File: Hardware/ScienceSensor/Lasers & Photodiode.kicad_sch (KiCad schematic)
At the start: 12 parts

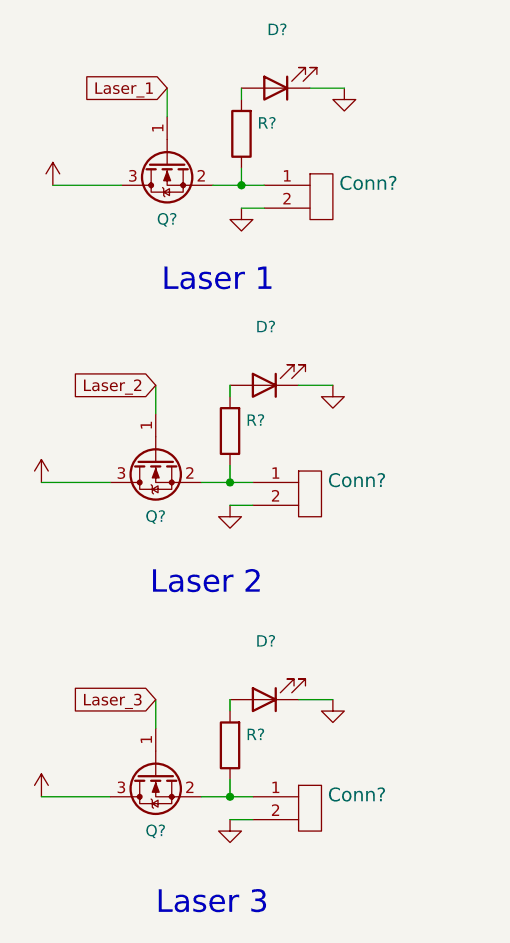
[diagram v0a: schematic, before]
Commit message: Created NO sensor, NH3 sensor, worked on Mosfets, and created Methane sensor with labels.
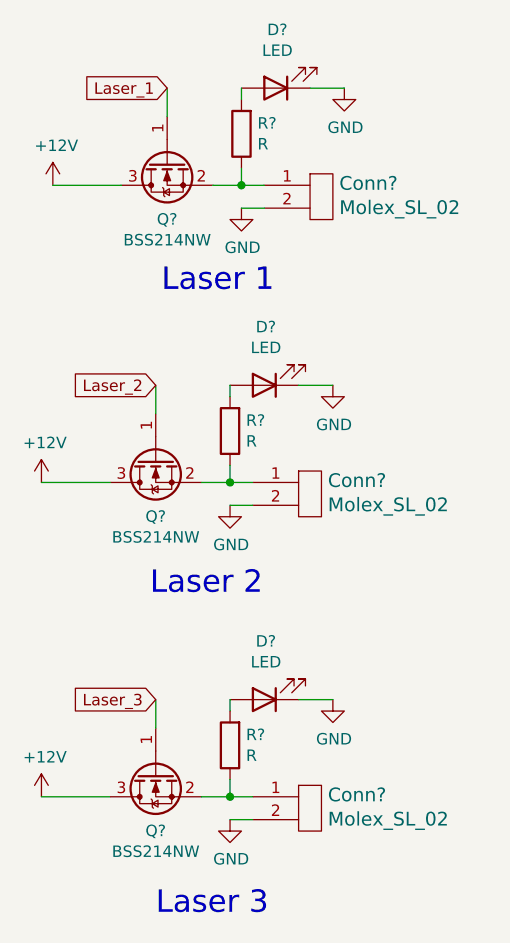
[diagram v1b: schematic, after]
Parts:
- Conn? (x3): value (none) -> Molex_SL_02
- D? (x3): value (none) -> LED
- Q? (x3): value (none) -> BSS214NW; footprint (none) -> Package_TO_SOT_SMD:SOT-323_SC-70
- R? (x3): value (none) -> R
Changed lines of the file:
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@@
     (in_bom yes) (on_board yes)
     (property "Reference" "Q?" (id 0) (at 38.1 42.5196 90))
-    (property "Value" "" (id 1) (at 38.1 44.831 90))
-    (property "Footprint" "" (id 2) (at 40.005 41.275 0)
+    (property "Value" "BSS214NW" (id 1) (at 38.1 44.831 90))
+    (property "Footprint" "Package_TO_SOT_SMD:SOT-323_SC-70" (id 2) (at 40.005 41.275 0)
       (effects (font (size 1.27 1.27) italic) (justify left) hide)
     )
@@
       (effects (font (size 1.524 1.524)) (justify left))
     )
-    (property "Value" "" (id 1) (at 57.2262 41.2242 0)
+    (property "Value" "Molex_SL_02" (id 1) (at 57.2262 41.2242 0)
       (effects (font (size 1.524 1.524)) (justify left))
     )
@@
       (effects (font (size 1.27 1.27)) hide)
     )
-    (property "Value" "" (id 1) (at 25.781 34.3408 0))
+    (property "Value" "+12V" (id 1) (at 25.781 34.3408 0))
     (property "Footprint" "" (id 2) (at 25.4 38.735 0)
       (effects (font (size 1.27 1.27)) hide)
@@
       (effects (font (size 1.27 1.27)) hide)
     )
-    (property "Value" "" (id 1) (at 46.482 45.6692 0))
+    (property "Value" "GND" (id 1) (at 46.482 45.6692 0))
     (property "Footprint" "" (id 2) (at 46.355 41.275 0)
       (effects (font (size 1.27 1.27)) hide)
@@
       (effects (font (size 1.27 1.27)) (justify right))
     )
-    (property "Value" "" (id 1) (at 48.133 34.163 0)
+    (property "Value" "R" (id 1) (at 48.133 34.163 0)
       (effects (font (size 1.27 1.27)) (justify right))
     )
@@
     (in_bom yes) (on_board yes)
     (property "Reference" "D?" (id 0) (at 50.3428 21.463 0))
-    (property "Value" "" (id 1) (at 50.3428 23.7744 0))
+    (property "Value" "LED" (id 1) (at 50.3428 23.7744 0))
     (property "Footprint" "" (id 2) (at 50.165 27.94 0)
       (effects (font (size 1.27 1.27)) hide)
@@
       (effects (font (size 1.27 1.27)) hide)
     )
-    (property "Value" "" (id 1) (at 57.912 32.3342 0))
+    (property "Value" "GND" (id 1) (at 57.912 32.3342 0))
     (property "Footprint" "" (id 2) (at 57.785 27.94 0)
       (effects (font (size 1.27 1.27)) hide)
@@
     (in_bom yes) (on_board yes)
     (property "Reference" "Q?" (id 0) (at 36.83 75.5396 90))
-    (property "Value" "" (id 1) (at 36.83 77.851 90))
-    (property "Footprint" "" (id 2) (at 38.735 74.295 0)
+    (property "Value" "BSS214NW" (id 1) (at 36.83 77.851 90))
+    (property "Footprint" "Package_TO_SOT_SMD:SOT-323_SC-70" (id 2) (at 38.735 74.295 0)
       (effects (font (size 1.27 1.27) italic) (justify left) hide)
     )
@@
       (effects (font (size 1.524 1.524)) (justify left))
     )
-    (property "Value" "" (id 1) (at 55.9562 74.2442 0)
+    (property "Value" "Molex_SL_02" (id 1) (at 55.9562 74.2442 0)
       (effects (font (size 1.524 1.524)) (justify left))
     )
@@
       (effects (font (size 1.27 1.27)) hide)
     )
-    (property "Value" "" (id 1) (at 24.511 67.3608 0))
+    (property "Value" "+12V" (id 1) (at 24.511 67.3608 0))
     (property "Footprint" "" (id 2) (at 24.13 71.755 0)
       (effects (font (size 1.27 1.27)) hide)
@@
       (effects (font (size 1.27 1.27)) hide)
     )
-    (property "Value" "" (id 1) (at 45.212 78.6892 0))
+    (property "Value" "GND" (id 1) (at 45.212 78.6892 0))
     (property "Footprint" "" (id 2) (at 45.085 74.295 0)
       (effects (font (size 1.27 1.27)) hide)
@@
       (effects (font (size 1.27 1.27)) (justify right))
     )
-    (property "Value" "" (id 1) (at 46.863 67.183 0)
+    (property "Value" "R" (id 1) (at 46.863 67.183 0)
       (effects (font (size 1.27 1.27)) (justify right))
     )
@@
     (in_bom yes) (on_board yes)
     (property "Reference" "D?" (id 0) (at 49.0728 54.483 0))
-    (property "Value" "" (id 1) (at 49.0728 56.7944 0))
+    (property "Value" "LED" (id 1) (at 49.0728 56.7944 0))
     (property "Footprint" "" (id 2) (at 48.895 60.96 0)
       (effects (font (size 1.27 1.27)) hide)
@@
       (effects (font (size 1.27 1.27)) hide)
     )
-    (property "Value" "" (id 1) (at 56.642 65.3542 0))
+    (property "Value" "GND" (id 1) (at 56.642 65.3542 0))
     (property "Footprint" "" (id 2) (at 56.515 60.96 0)
       (effects (font (size 1.27 1.27)) hide)
@@
     (in_bom yes) (on_board yes)
     (property "Reference" "Q?" (id 0) (at 36.83 110.4646 90))
-    (property "Value" "" (id 1) (at 36.83 112.776 90))
-    (property "Footprint" "" (id 2) (at 38.735 109.22 0)
+    (property "Value" "BSS214NW" (id 1) (at 36.83 112.776 90))
+    (property "Footprint" "Package_TO_SOT_SMD:SOT-323_SC-70" (id 2) (at 38.735 109.22 0)
       (effects (font (size 1.27 1.27) italic) (justify left) hide)
     )
@@
       (effects (font (size 1.524 1.524)) (justify left))
     )
-    (property "Value" "" (id 1) (at 55.9562 109.1692 0)
+    (property "Value" "Molex_SL_02" (id 1) (at 55.9562 109.1692 0)
       (effects (font (size 1.524 1.524)) (justify left))
     )
@@
       (effects (font (size 1.27 1.27)) hide)
     )
-    (property "Value" "" (id 1) (at 24.511 102.2858 0))
+    (property "Value" "+12V" (id 1) (at 24.511 102.2858 0))
     (property "Footprint" "" (id 2) (at 24.13 106.68 0)
       (effects (font (size 1.27 1.27)) hide)
@@
       (effects (font (size 1.27 1.27)) hide)
     )
-    (property "Value" "" (id 1) (at 45.212 113.6142 0))
+    (property "Value" "GND" (id 1) (at 45.212 113.6142 0))
     (property "Footprint" "" (id 2) (at 45.085 109.22 0)
       (effects (font (size 1.27 1.27)) hide)
@@
       (effects (font (size 1.27 1.27)) (justify right))
     )
-    (property "Value" "" (id 1) (at 46.863 102.108 0)
+    (property "Value" "R" (id 1) (at 46.863 102.108 0)
       (effects (font (size 1.27 1.27)) (justify right))
     )
@@
     (in_bom yes) (on_board yes)
     (property "Reference" "D?" (id 0) (at 49.0728 89.408 0))
-    (property "Value" "" (id 1) (at 49.0728 91.7194 0))
+    (property "Value" "LED" (id 1) (at 49.0728 91.7194 0))
     (property "Footprint" "" (id 2) (at 48.895 95.885 0)
       (effects (font (size 1.27 1.27)) hide)
@@
       (effects (font (size 1.27 1.27)) hide)
     )
-    (property "Value" "" (id 1) (at 56.642 100.2792 0))
+    (property "Value" "GND" (id 1) (at 56.642 100.2792 0))
     (property "Footprint" "" (id 2) (at 56.515 95.885 0)
       (effects (font (size 1.27 1.27)) hide)

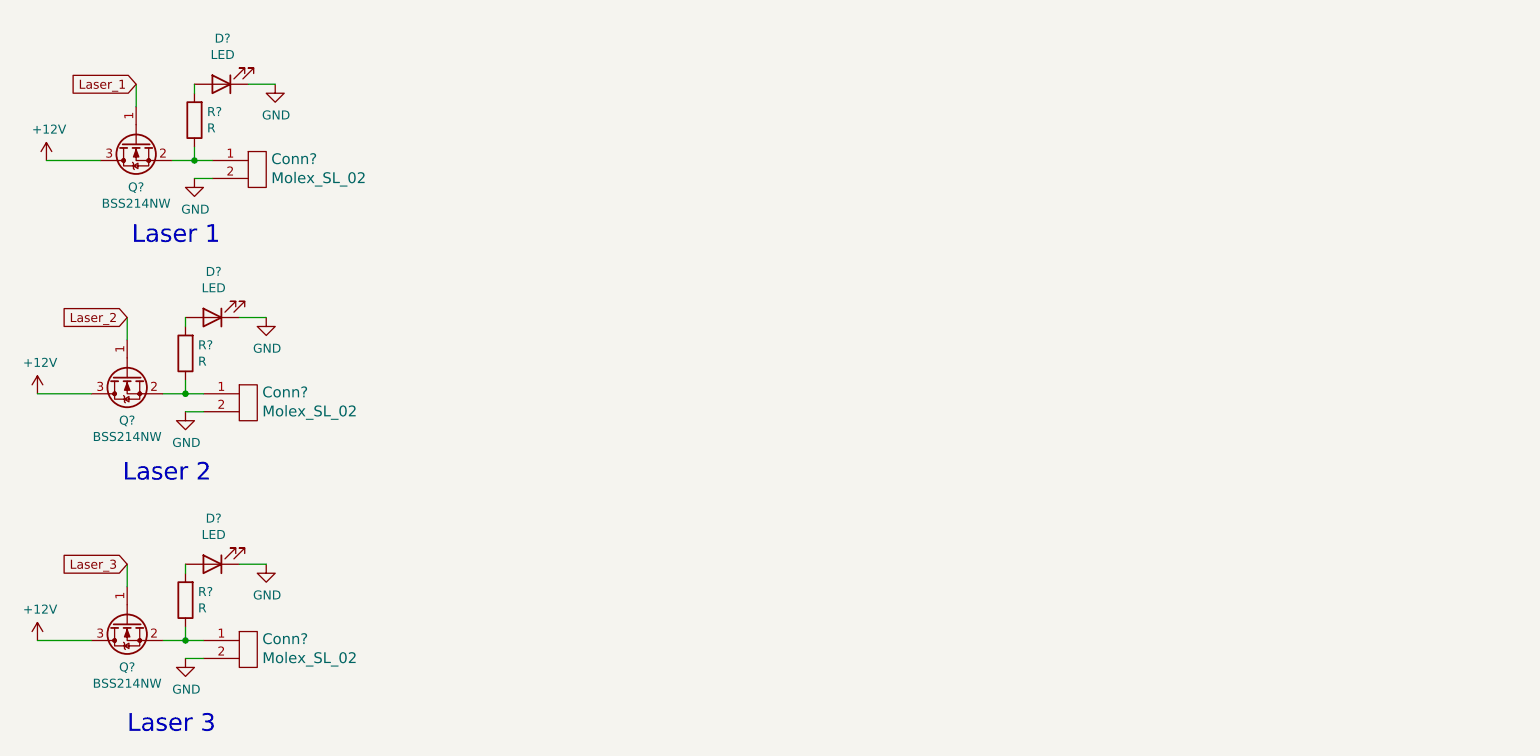
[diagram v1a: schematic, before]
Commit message: BOM generated, photodiodes added
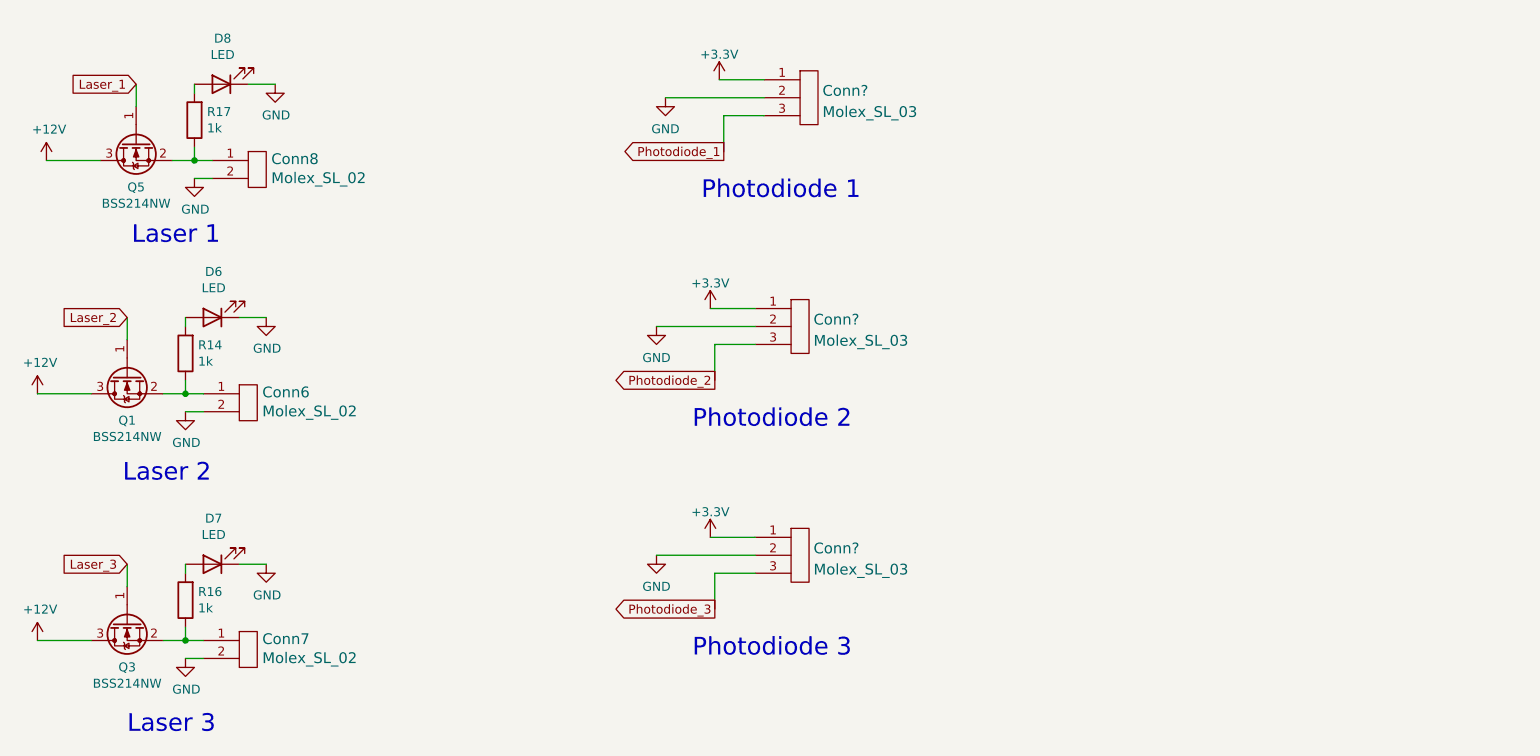
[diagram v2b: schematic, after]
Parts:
- added Conn? (x3): Molex_SL_03, symbol MRDT_Connectors:Molex_SL_03
- R14, R16, R17: renamed from R?; value R -> 1k
- gave numbers to parts that had none: 9
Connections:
- net GND: now also Conn?.2, Conn?.2, Conn?.2
- new net +3.3V: Conn?.1, Conn?.1, Conn?.1
- new net Photodiode_1: Conn?.3
- new net Photodiode_2: Conn?.3
- new net Photodiode_3: Conn?.3
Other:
- note added: "Photodiode 1"
- note added: "Photodiode 2"
- note added: "Photodiode 3"

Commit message: Fixed diode ref / values
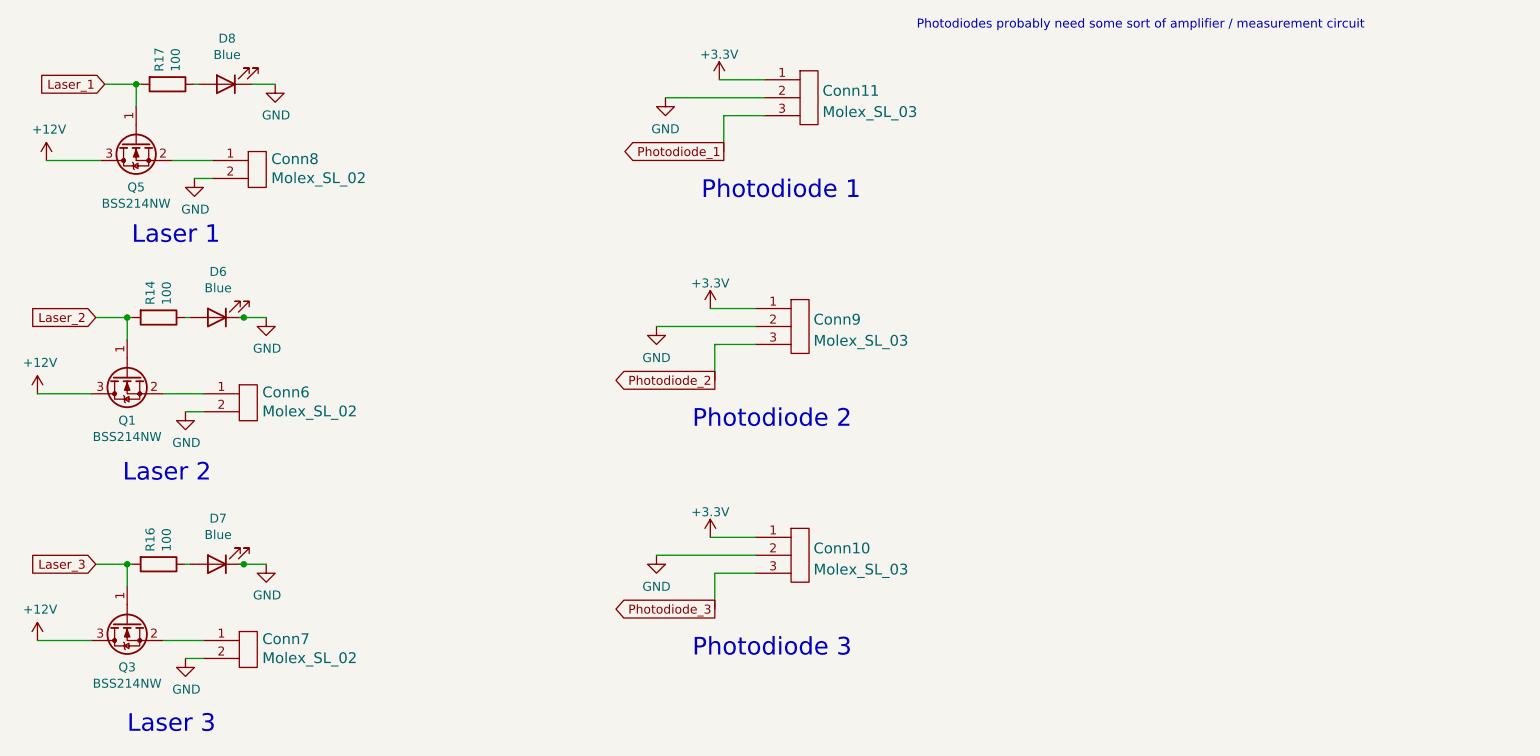
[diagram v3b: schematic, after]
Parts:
- D6, D7, D8: value LED -> Blue
- R14, R16, R17: value 1k -> 100
- gave numbers to parts that had none: 3
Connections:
- net Laser_1: now also R17.2
- net Laser_2: now also R14.2
- net Laser_3: now also R16.2
- net at Conn8.1, Q5.2 (S): no longer R17.1
- net at D8.2 (A): now also R17.1; no longer R17.2
- net at Conn6.1, Q1.2 (S): no longer R14.1
- net at D6.2 (A): now also R14.1; no longer R14.2
- net at Conn7.1, Q3.2 (S): no longer R16.1
- net at D7.2 (A): now also R16.1; no longer R16.2
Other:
- note added: "Photodiodes probably need some sort of amplifier / measurement circuit"
- moved on the sheet: D6, D7, D8, R14, R16, R17

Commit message: Schematic Review
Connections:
- net +12V: no longer Q5.3 (D)
- net GND: no longer Conn8.2
- net Laser_1: no longer Q5.1 (G)
- net at Q5.2 (S): no longer Conn8.1
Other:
- moved on the sheet: Q5
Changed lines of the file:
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@@
 (kicad_sch (version 20211123) (generator eeschema)
   (paper "A4")
-  (junction (at 38.1 27.94) (diameter 0) (color 0 0 0 0)
-  )
   (junction (at 36.83 60.96) (diameter 0) (color 0 0 0 0)
   )
@@
   (junction (at 53.34 60.96) (diameter 0) (color 0 0 0 0)
   )
-  (wire (pts (xy 33.655 27.94) (xy 38.1 27.94))
+  (wire (pts (xy 33.655 27.94) (xy 38.735 27.94))
     (stroke (width 0) (type default) (color 0 0 0 0))
   )
@@
     (stroke (width 0) (type default) (color 0 0 0 0))
   )
-  (wire (pts (xy 38.1 31.115) (xy 38.1 27.94))
-    (stroke (width 0) (type default) (color 0 0 0 0))
-  )
-  (wire (pts (xy 38.1 27.94) (xy 38.735 27.94))
-    (stroke (width 0) (type default) (color 0 0 0 0))
-  )
   (wire (pts (xy 120.65 27.305) (xy 127 27.305))
     (stroke (width 0) (type default) (color 0 0 0 0))
@@
     (stroke (width 0) (type default) (color 0 0 0 0))
   )
-  (wire (pts (xy 25.4 38.735) (xy 33.02 38.735))
-    (stroke (width 0) (type default) (color 0 0 0 0))
-  )
   (wire (pts (xy 45.085 74.295) (xy 47.625 74.295))
     (stroke (width 0) (type default) (color 0 0 0 0))
@@
   )
   (wire (pts (xy 121.285 32.385) (xy 121.285 37.465))
-    (stroke (width 0) (type default) (color 0 0 0 0))
-  )
-  (wire (pts (xy 43.18 38.735) (xy 48.895 38.735))
     (stroke (width 0) (type default) (color 0 0 0 0))
   )
@@
     )
   )
-  (symbol (lib_id "Transistor_FET:BSS214NW") (at 38.1 36.195 90) (mirror x) (unit 1)
-    (in_bom yes) (on_board yes)
-    (property "Reference" "Q5" (id 0) (at 38.1 42.5196 90))
-    (property "Value" "BSS214NW" (id 1) (at 38.1 44.831 90))
-    (property "Footprint" "Package_TO_SOT_SMD:SOT-323_SC-70" (id 2) (at 40.005 41.275 0)
+  (symbol (lib_id "Transistor_FET:BSS214NW") (at 35.56 36.195 0) (mirror x) (unit 1)
+    (in_bom yes) (on_board yes)
+    (property "Reference" "Q5" (id 0) (at 41.8846 36.195 90))
+    (property "Value" "BSS214NW" (id 1) (at 44.196 36.195 90))
+    (property "Footprint" "Package_TO_SOT_SMD:SOT-323_SC-70" (id 2) (at 40.64 34.29 0)
       (effects (font (size 1.27 1.27) italic) (justify left) hide)
     )
-    (property "Datasheet" "https://www.infineon.com/dgdl/Infineon-BSS214NW-DS-v02_02-en.pdf?fileId=db3a30431b3e89eb011b695aebc01bde" (id 3) (at 38.1 36.195 0)
+    (property "Datasheet" "https://www.infineon.com/dgdl/Infineon-BSS214NW-DS-v02_02-en.pdf?fileId=db3a30431b3e89eb011b695aebc01bde" (id 3) (at 35.56 36.195 0)
       (effects (font (size 1.27 1.27)) (justify left) hide)
     )
@@
     (pin "1")
   )
-  (symbol (lib_id "power:GND") (at 46.355 41.275 0) (unit 1)
-    (in_bom yes) (on_board yes)
-    (property "Reference" "#PWR049" (id 0) (at 46.355 47.625 0)
-      (effects (font (size 1.27 1.27)) hide)
-    )
-    (property "Value" "GND" (id 1) (at 46.482 45.6692 0))
-    (property "Footprint" "" (id 2) (at 46.355 41.275 0)
-      (effects (font (size 1.27 1.27)) hide)
-    )
-    (property "Datasheet" "" (id 3) (at 46.355 41.275 0)
-      (effects (font (size 1.27 1.27)) hide)
-    )
+  (symbol (lib_id "power:GND") (at 25.4 41.275 0) (unit 1)
+    (in_bom yes) (on_board yes)
+    (property "Reference" "#PWR049" (id 0) (at 25.4 47.625 0)
+      (effects (font (size 1.27 1.27)) hide)
+    )
+    (property "Value" "GND" (id 1) (at 25.527 45.6692 0))
+    (property "Footprint" "" (id 2) (at 25.4 41.275 0)
+      (effects (font (size 1.27 1.27)) hide)
+    )
+    (property "Datasheet" "" (id 3) (at 25.4 41.275 0)
+      (effects (font (size 1.27 1.27)) hide)
+    )
